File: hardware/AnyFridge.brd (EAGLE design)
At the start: 100 x 80 mm, 11 parts

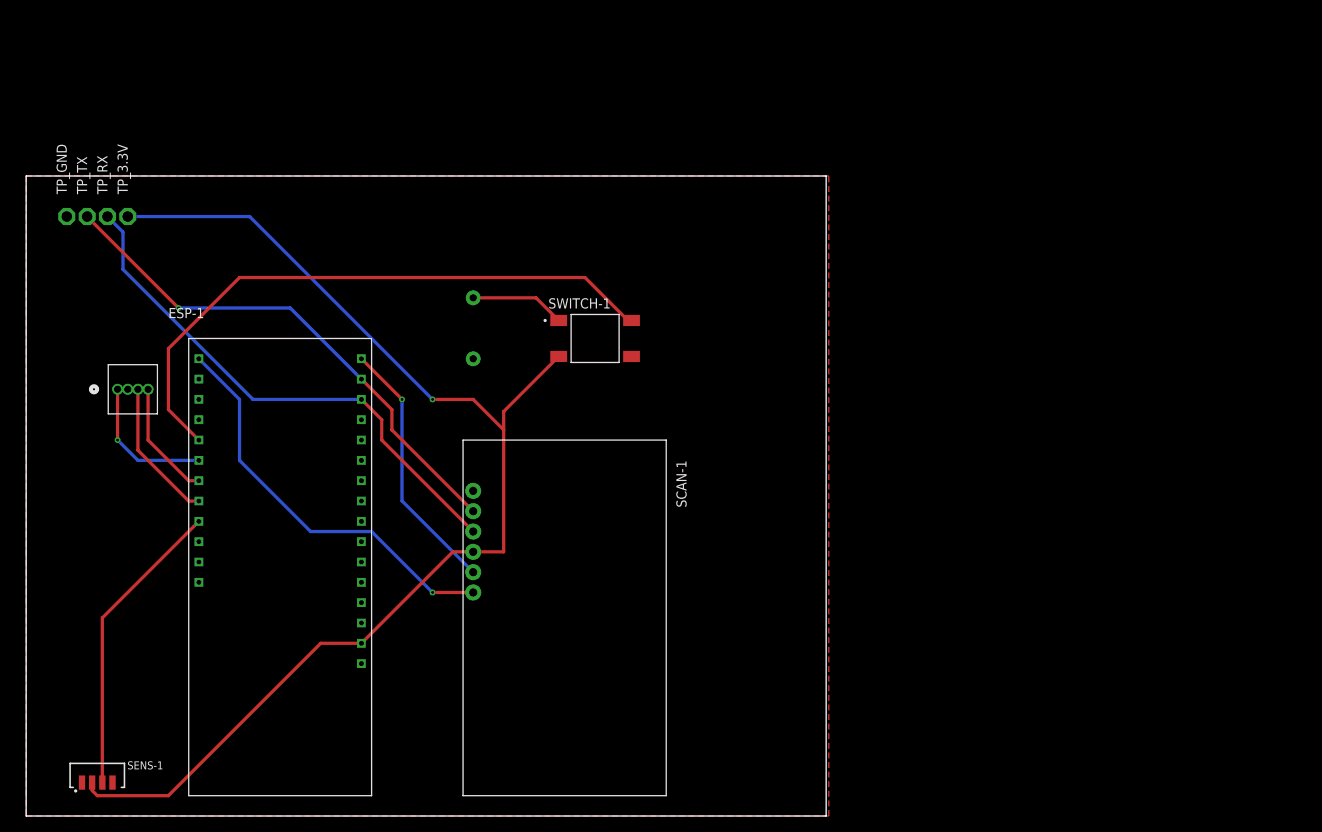
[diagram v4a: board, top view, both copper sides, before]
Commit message: Make PCB much smaller
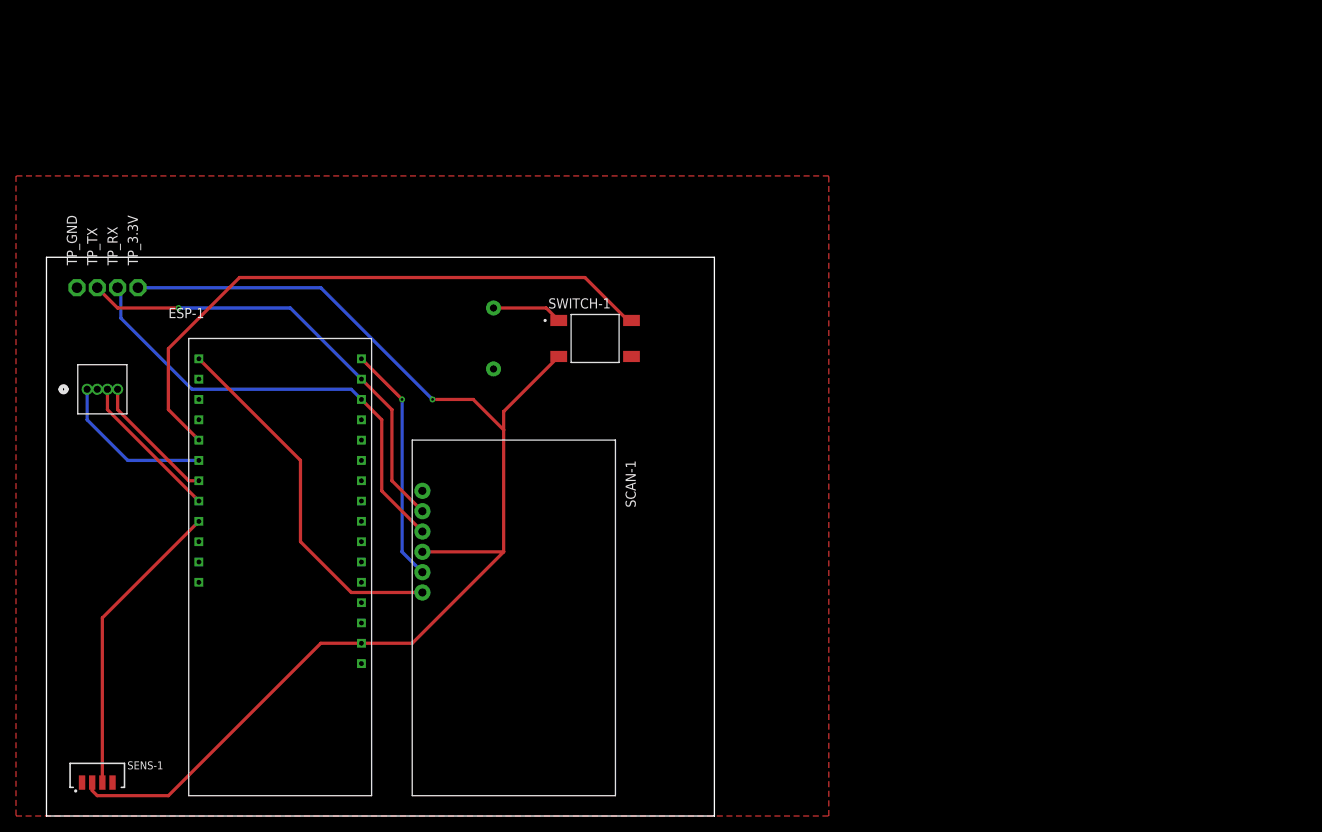
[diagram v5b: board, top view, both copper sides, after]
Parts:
- moved TP_3.3V 8.98 mm to (14.0, 66.0)
- moved TP_GND 8.98 mm to (6.35, 66.0)
- moved TP_RX 8.98 mm to (11.4, 66.0)
- moved TP_TX 8.98 mm to (8.89, 66.0)
- moved SCAN-1 6.35 mm to (73.7, 47.0)
- moved LED-1 3.81 mm to (7.62, 53.3)
- moved R1 2.84 mm to (58.4, 59.7)
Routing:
- net RX1: track 66.3 -> 57.9 mm
- net TX1: track 65.0 -> 57.4 mm
- net 3.3V: track 150.6 -> 155.8 mm
- net STAT: track 50.9 -> 46.0 mm, vias 1 -> 0
- net N$1: track 11.9 -> 8.80 mm
- net TRIG: track 32.5 -> 29.8 mm
- net RED: track 17.6 -> 19.9 mm, vias 1 -> 0
- net GREEN: track 14.8 -> 16.4 mm
- net BLUE: track 17.9 -> 18.7 mm
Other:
- board size 100 x 80 mm -> 83.5 x 69.8 mm
